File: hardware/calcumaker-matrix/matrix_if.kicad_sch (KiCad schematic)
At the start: 2 parts, among them J1 TO MCU (unified SPI FFC)

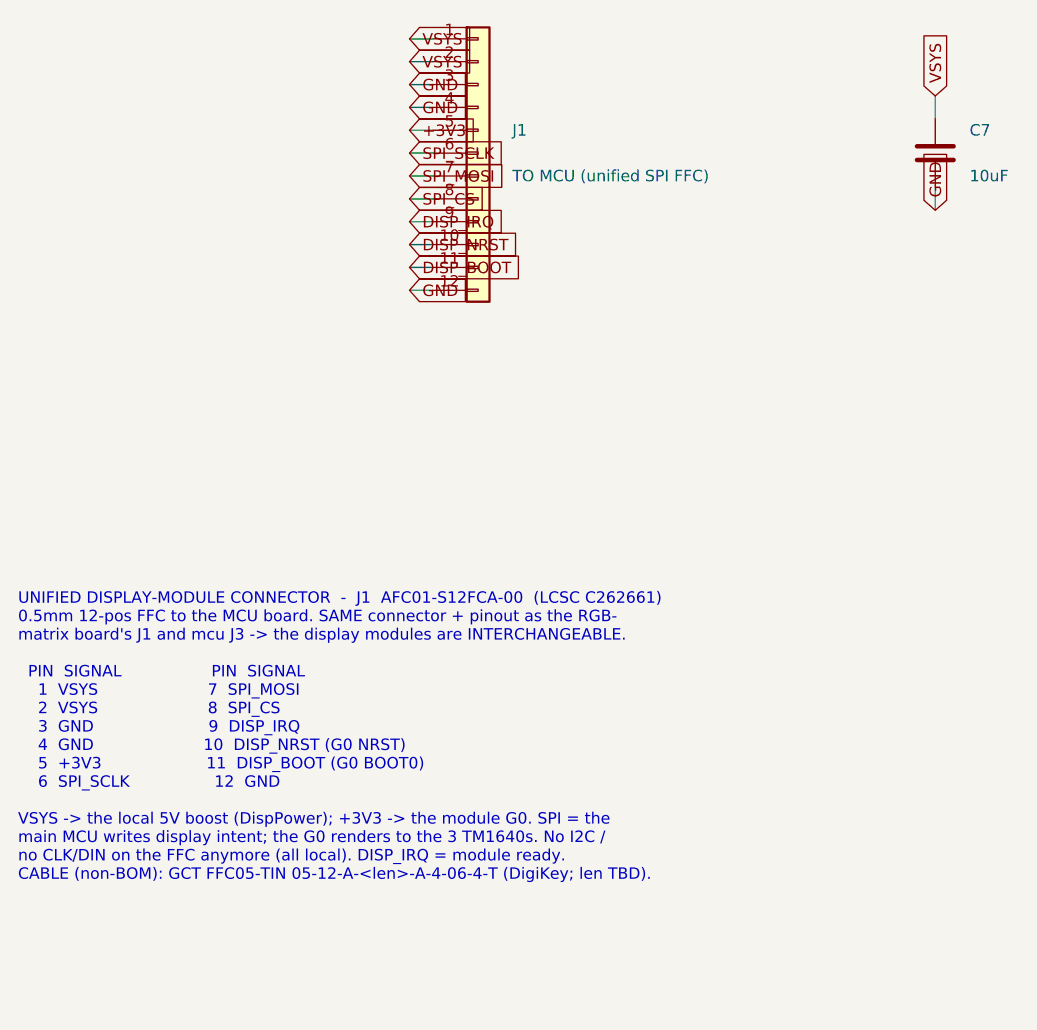
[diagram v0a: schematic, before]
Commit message: hardware: unified SPI display-module interface + RGB dot-matrix board
Make the display a swappable module on ONE technology-agnostic connector
(mirrors the keyboard-G0 pattern): the MCU board speaks a single SPI
"display intent" bus and each display board carries its own MCU that
renders locally. Two interchangeable modules on the same 12-pin FFC.

- calcumaker-matrix (NEW): full-color RGB dot matrix, 96x24 = 2304x 1mm
  XL-1010RGBC-2812B-S (C51900942) driven by an RP2040 (PIO). Nested
  multi-channel: led_cluster (8x8) x12 -> led_row (768px chain) x3.
  Dedicated VSYS LED-power inlet keeps amps off the signal FFC. Authored
  the 1mm 1010 footprint; RP2040/flash/shifter symbols are stock.
- calcumaker-display (7-seg): retrofit to a smart module -- added an
  STM32G031 SPI slave, and moved the 5V boost (TPS61022) + 74HCT125
  shifter off the MCU board onto it. Interconnect reworked CLK/DIN -> SPI.
- calcumaker-mcu: DisplayIF simplified to the unified SPI connector +
  a 2-pin VSYS outlet for the matrix LED rail.

Unified pinout (mcu J3 / display J1 / matrix J1): VSYS,VSYS,GND,GND,+3V3,
SPI_SCLK,SPI_MOSI,SPI_CS,DISP_IRQ,DISP_NRST,DISP_BOOT,GND.

All boards generate + check clean (mcu 46 / keyboard 179 / display 77 /
matrix 2339, no dup refs). Docs (PARTS.md, DESIGN.md, Makefile) updated.
Firmware is deferred; the SPI contract is documented so it is unblocked.

Co-Authored-By: Claude Opus 4.8 (1M context) <noreply@anthropic.com>
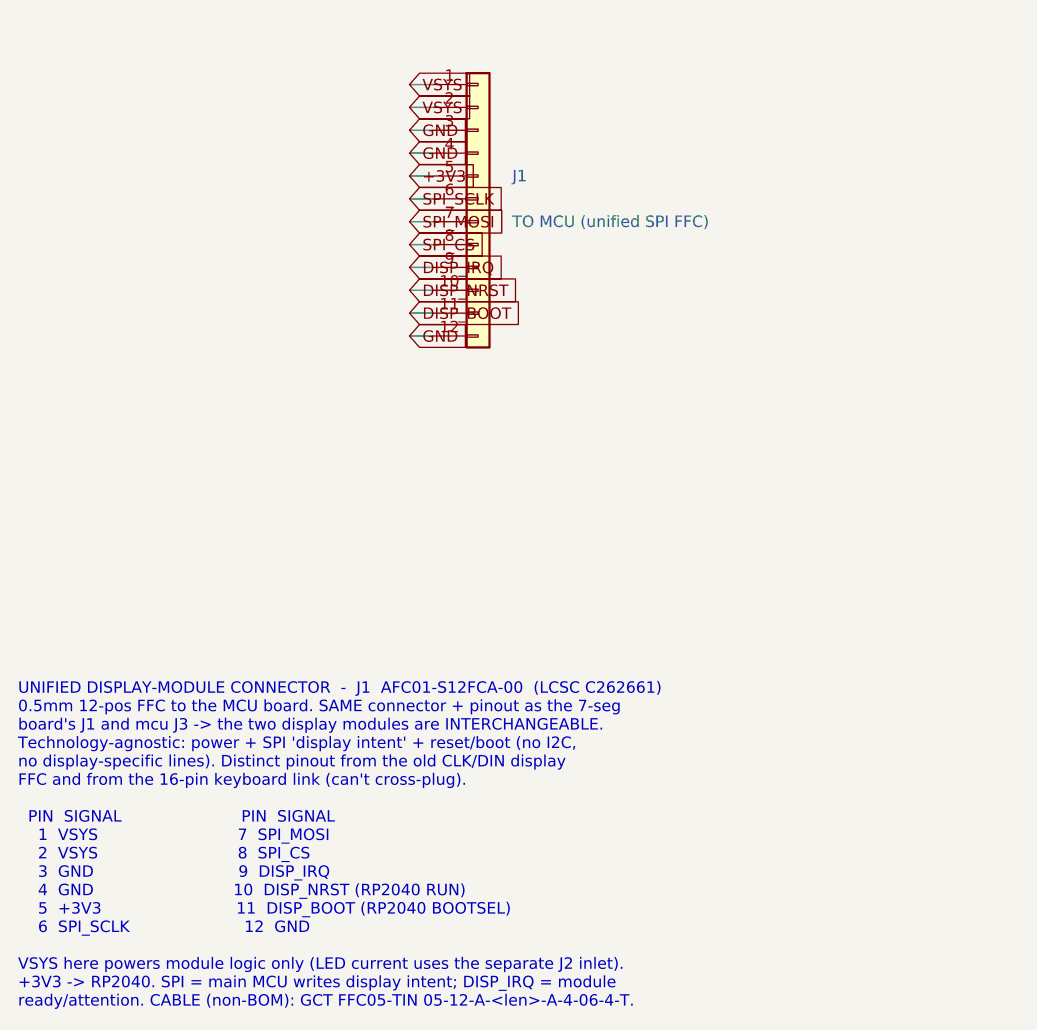
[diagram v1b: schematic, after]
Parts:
- removed C7: 10uF, Capacitor_SMD:C_0603_1608Metric, symbol Device:C
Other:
- note added: "UNIFIED DISPLAY-MODULE CONNECTOR - J1 AFC01-S12FCA-00 (LCSC C262661) 0.5mm 12-pos FFC to the MCU board. SAME connector + pinout as the 7-seg board's J1 and mcu J3 -> the two display modules are INTERCHANGEABLE. Technology-agnostic: power + SPI 'display intent' + reset/boot (no I2C, no display-specific lines). Distinct pinout from the old CLK/DIN display FFC and from the 16-pin keyboard link (can'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"
- note removed: "UNIFIED DISPLAY-MODULE CONNECTOR - J1 AFC01-S12FCA-00 (LCSC C262661) 0.5mm 12-pos FFC to the MCU board. SAME connector + pinout as the RGB- matrix board's J1 and mcu J3 -> the display modules are INTERCHANGEABLE. PIN SIGNAL PIN SIGNAL 1 VSYS 7 SPI_MOSI 2 VSYS 8 SPI_CS 3 GND 9 DISP_IRQ 4 GND 10 DISP_NRST (G0 NRST) 5 +3V3 11 DISP_BOOT (G0 BOOT0) 6 SPI_SCLK 12 GND VSYS -> the local 5V boost (DispPow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"
- title: Calcumaker 16 — Display — MCU board interconnect (0.5mm FFC) -> Calcumaker 16 — RGB Matrix — Unified SPI display-module connector (0.5mm FFC)
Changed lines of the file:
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@@
 	(paper "A3")
 	(title_block
-		(title "Calcumaker 16 — Display — MCU board interconnect (0.5mm FFC)")
-		(date "2026-07-04")
-		(rev "0.2")
+		(title "Calcumaker 16 — RGB Matrix — Unified SPI display-module connector (0.5mm FFC)")
+		(date "2026-07-07")
+		(rev "0.1")
 		(company "calcumaker authors")
 	)
 	(symbol
 		(lib_id "Connector_Generic:Conn_01x12")
-		(at 71.1200 71.1200 0)
+		(at 71.1200 76.2000 0)
 		(unit 1)
 		(exclude_from_sim no)
@@
 		(dnp no)
 		(property "Reference" "J1"
-			(at 74.9300 68.5800 0)
+			(at 74.9300 73.6600 0)
 			(effects (font (size 1.27 1.27)) (justify left))
 		)
 		(property "Value" "TO MCU (unified SPI FFC)"
-			(at 74.9300 73.6600 0)
+			(at 74.9300 78.7400 0)
 			(effects (font (size 1.27 1.27)) (justify left))
 		)
 		(property "Footprint" "Connector_FFC-FPC:Hirose_FH12-12S-0.5SH_1x12-1MP_P0.50mm_Horizontal"
-			(at 71.1200 71.1200 0)
+			(at 71.1200 76.2000 0)
 			(effects (font (size 1.27 1.27))) (hide yes)
 		)
 		(property "Datasheet" "~"
-			(at 71.1200 71.1200 0)
+			(at 71.1200 76.2000 0)
 			(effects (font (size 1.27 1.27))) (hide yes)
 		)
 		(property "LCSC" "C262661"
-			(at 71.1200 71.1200 0)
+			(at 71.1200 76.2000 0)
 			(effects (font (size 1.27 1.27))) (hide yes)
 		)
 		(property "MPN" "AFC01-S12FCA-00"
-			(at 71.1200 71.1200 0)
+			(at 71.1200 76.2000 0)
 			(effects (font (size 1.27 1.27))) (hide yes)
 		)
 		(property "Manufacturer" "JUSHUO"
-			(at 71.1200 71.1200 0)
+			(at 71.1200 76.2000 0)
 			(effects (font (size 1.27 1.27))) (hide yes)
 		)
@@
 		(pin "12")
 		(instances
-			(project "calcumaker-display"
-				(path "/ca1c0000-0000-4000-8000-0000000d1501/ca1c0000-0000-4000-8000-0000000d1520"
+			(project "calcumaker-matrix"
+				(path "/ca1c0000-0000-4000-8000-0000000d3001/ca1c0000-0000-4000-8000-0000000d3220"
 					(reference "J1")
 					(unit 1)
@@
 		)
 	)
-	(symbol
-		(lib_id "Device:C")
-		(at 121.9200 71.1200 0)
-		(unit 1)
-		(exclude_from_sim no)
-		(in_bom yes)
-		(on_board yes)
-		(dnp no)
-		(property "Reference" "C7"
-			(at 125.7300 68.5800 0)
-			(effects (font (size 1.27 1.27)) (justify left))
-		)
-		(property "Value" "10uF"
-			(at 125.7300 73.6600 0)
-			(effects (font (size 1.27 1.27)) (justify left))
-		)
-		(property "Footprint" "Capacitor_SMD:C_0603_1608Metric"
-			(at 121.9200 71.1200 0)
-			(effects (font (size 1.27 1.27))) (hide yes)
-		)
-		(property "Datasheet" "~"
-			(at 121.9200 71.1200 0)
-			(effects (font (size 1.27 1.27))) (hide yes)
-		)
-		(property "LCSC" "C15850"
-			(at 121.9200 71.1200 0)
-			(effects (font (size 1.27 1.27))) (hide yes)
-		)
-		(pin "1")
-		(pin "2")
-		(instances
-			(project "calcumaker-display"
-				(path "/ca1c0000-0000-4000-8000-0000000d1501/ca1c0000-0000-4000-8000-0000000d1520"
-					(reference "C7")
-					(unit 1)
-				)
-			)
-		)
-	)
-	(wire (pts (xy 66.0400 58.4200) (xy 63.5000 58.4200))
+	(wire (pts (xy 66.0400 63.5000) (xy 63.5000 63.5000))
 		(stroke (width 0) (type default))
 	)
 	(global_label "VSYS"
-		(shape input)
-		(at 63.5000 58.4200 180)
-		(fields_autoplaced yes)
-		(effects (font (size 1.27 1.27)) (justify left))
-	)
-	(wire (pts (xy 66.0400 60.9600) (xy 63.5000 60.9600))
-		(stroke (width 0) (type default))
-	)
-	(global_label "VSYS"
-		(shape input)
-		(at 63.5000 60.9600 180)
-		(fields_autoplaced yes)
-		(effects (font (size 1.27 1.27)) (justify left))
-	)
-	(wire (pts (xy 66.0400 63.5000) (xy 63.5000 63.5000))
-		(stroke (width 0) (type default))
-	)
-	(global_label "GND"
 		(shape input)
 		(at 63.5000 63.5000 180)
@@
 		(stroke (width 0) (type default))
 	)
-	(global_label "GND"
+	(global_label "VSYS"
 		(shape input)
 		(at 63.5000 66.0400 180)
@@
 		(stroke (width 0) (type default))
 	)
-	(global_label "+3V3"
+	(global_label "GND"
 		(shape input)
 		(at 63.5000 68.5800 180)
@@
 		(stroke (width 0) (type default))
 	)
-	(global_label "SPI_SCLK"
+	(global_label "GND"
 		(shape input)
 		(at 63.5000 71.1200 180)
@@
 		(stroke (width 0) (type default))
 	)
-	(global_label "SPI_MOSI"
+	(global_label "+3V3"
 		(shape input)
 		(at 63.5000 73.6600 180)
@@
 		(stroke (width 0) (type default))
 	)
-	(global_label "SPI_CS"
+	(global_label "SPI_SCLK"
 		(shape input)
 		(at 63.5000 76.2000 180)
@@
 		(stroke (width 0) (type default))
 	)
-	(global_label "DISP_IRQ"
+	(global_label "SPI_MOSI"
 		(shape input)
 		(at 63.5000 78.7400 180)
@@
 		(stroke (width 0) (type default))
 	)
-	(global_label "DISP_NRST"
+	(global_label "SPI_CS"
 		(shape input)
 		(at 63.5000 81.2800 180)
@@
 		(stroke (width 0) (type default))
 	)
-	(global_label "DISP_BOOT"
+	(global_label "DISP_IRQ"
 		(shape input)
 		(at 63.5000 83.8200 180)
@@
 		(stroke (width 0) (type default))
 	)
-	(global_label "GND"
+	(global_label "DISP_NRST"
 		(shape input)
 		(at 63.5000 86.3600 180)
@@
 		(effects (font (size 1.27 1.27)) (justify left))
 	)
-	(wire (pts (xy 121.9200 67.3100) (xy 121.9200 64.7700))
+	(wire (pts (xy 66.0400 88.9000) (xy 63.5000 88.9000))
 		(stroke (width 0) (type default))
 	)
-	(global_label "VSYS"
+	(global_label "DISP_BOOT"
 		(shape input)
-		(at 121.9200 64.7700 270)
+		(at 63.5000 88.9000 180)
 		(fields_autoplaced yes)
 		(effects (font (size 1.27 1.27)) (justify left))
 	)
-	(wire (pts (xy 121.9200 74.9300) (xy 121.9200 77.4700))
+	(wire (pts (xy 66.0400 91.4400) (xy 63.5000 91.4400))
 		(stroke (width 0) (type default))
 	)
 	(global_label "GND"
 		(shape input)
-		(at 121.9200 77.4700 90)
+		(at 63.5000 91.4400 180)
 		(fields_autoplaced yes)
 		(effects (font (size 1.27 1.27)) (justify left))
 	)
-	(text "UNIFIED DISPLAY-MODULE CONNECTOR  -  J1  AFC01-S12FCA-00  (LCSC C262661)\n0.5mm 12-pos FFC to the MCU board. SAME connector + pinout as the RGB-\nmatrix board's J1 and mcu J3 -> the display modules are INTERCHANGEABLE.\n\n  PIN  SIGNAL                  PIN  SIGNAL              \n    1  VSYS                      7  SPI_MOSI            \n    2  VSYS                      8  SPI_CS              \n    3  GND                       9  DISP_IRQ            \n    4  GND                      10  DISP_NRST (G0 NRST) \n    5  +3V3                     11  DISP_BOOT (G0 BOOT0)\n    6  SPI_SCLK                 12  GND\n\nVSYS -> the local 5V boost (DispPower); +3V3 -> the module G0. SPI = the\nmain MCU writes display intent; the G0 renders to the 3 TM1640s. No I2C /\nno CLK/DIN on the FFC anymore (all local). DISP_IRQ = module ready.\nCABLE (non-BOM): GCT FFC05-TIN 05-12-A-<len>-A-4-06-4-T (DigiKey; len TBD)."
+	(text "UNIFIED DISPLAY-MODULE CONNECTOR  -  J1  AFC01-S12FCA-00  (LCSC C262661)\n0.5mm 12-pos FFC to the MCU board. SAME connector + pinout as the 7-seg\nboard's J1 and mcu J3 -> the two display modules are INTERCHANGEABLE.\nTechnology-agnostic: power + SPI 'display intent' + reset/boot (no I2C,\nno display-specific lines). Distinct pinout from the old CLK/DIN display\nFFC and from the 16-pin keyboard link (can't cross-plug).\n\n  PIN  SIGNAL                        PIN  SIGNAL                    \n    1  VSYS                            7  SPI_MOSI                  \n    2  VSYS                            8  SPI_CS                    \n    3  GND                             9  DISP_IRQ                  \n    4  GND                            10  DISP_NRST (RP2040 RUN)    \n    5  +3V3                           11  DISP_BOOT (RP2040 BOOTSEL)\n    6  SPI_SCLK                       12  GND\n\nVSYS here powers module logic only (LED current uses the separate J2 inlet).\n+3V3 -> RP2040. SPI = main MCU writes display intent; DISP_IRQ = module\nready/attention. CABLE (non-BOM): GCT FFC05-TIN 05-12-A-<len>-A-4-06-4-T."
 		(exclude_from_sim no)
-		(at 20.00 120.00 0)
+		(at 20.00 130.00 0)
 		(effects (font (face "Courier New") (size 1.27 1.27)) (justify left top))
 	)
 	(sheet_instances
 		(path "/"
-			(page "6")
+			(page "5")
 		)
 	)
